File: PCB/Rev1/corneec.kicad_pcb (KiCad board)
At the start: 2 copper layers, 133.8 x 91.4 mm, 53 parts, among them J1 OLED, J2 MJ-4PP-9, Q1 Q_NMOS_GSD, SW1 SW_Push, SW10 EC_SW, SW11 EC_SW, SW12 EC_SW, SW13 EC_SW, SW14 EC_SW, SW15 EC_SW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

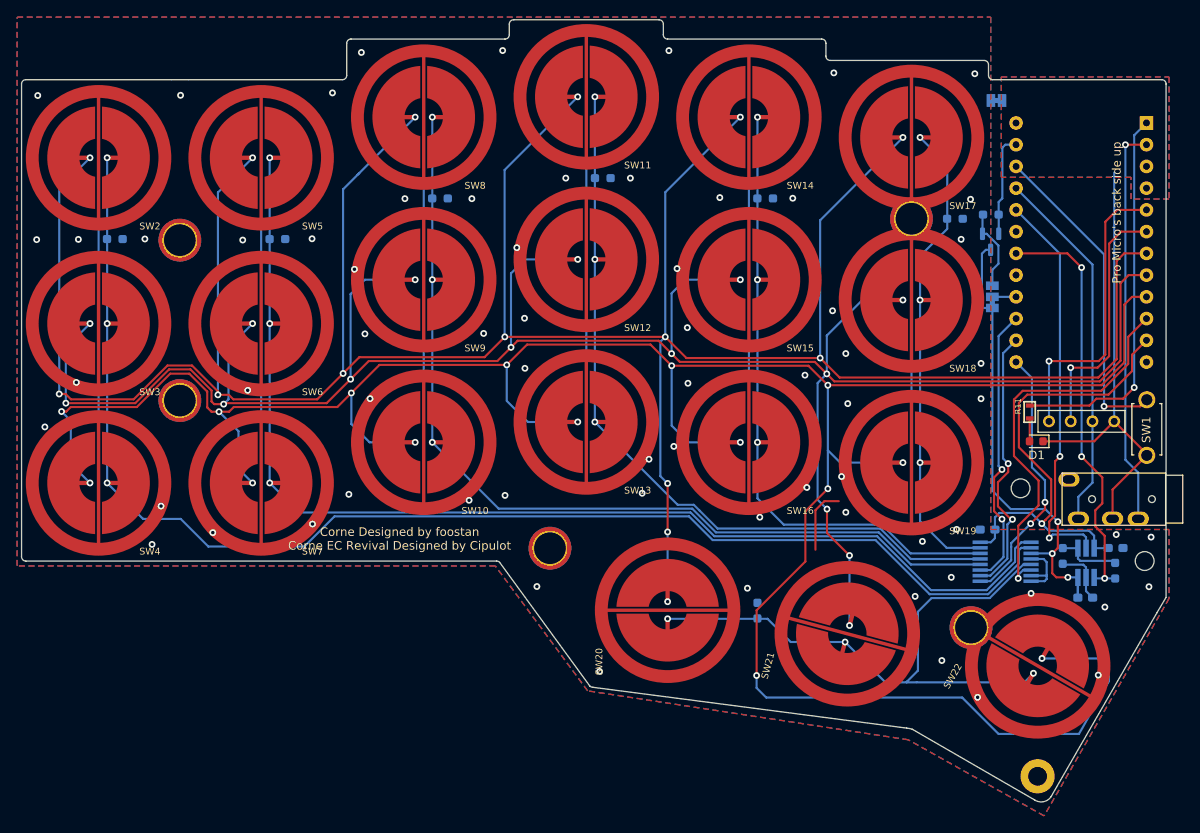
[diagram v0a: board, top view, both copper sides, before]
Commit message: FIX Production files
Fix to the production files that caused one of the 2 EC pads to be merged with the ground plane.
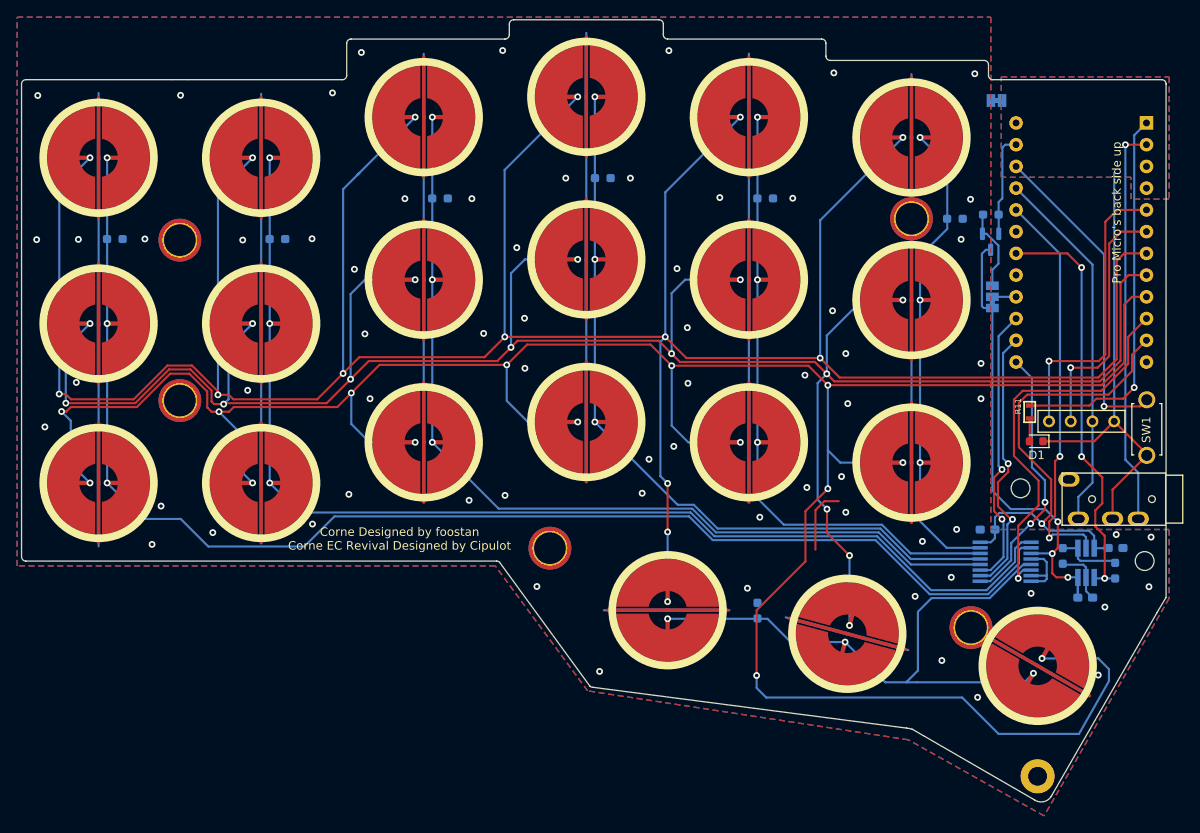
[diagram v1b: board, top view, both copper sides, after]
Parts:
- SW10, SW11, SW12, SW13, SW14, SW15, SW16, SW17, SW18, SW19, SW2, SW20, SW21, SW22, SW3, SW4, SW5, SW6, SW7, SW8, SW9: footprint cipulot_parts:ecs_pad -> cipulot_parts:ecs_pad_no_ring
